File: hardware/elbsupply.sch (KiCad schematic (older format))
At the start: 69 parts

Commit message: changed pre-regulator to TPS54331DDA, need to calculate exact values
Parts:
- removed C?: 100uF, symbol CP1
- removed C?: CP1, symbol CP1
- removed D?: DIODESCH, symbol DIODESCH
- removed D?: 1N4148WS, symbol DIODE
- removed L?: INDUCTOR, symbol INDUCTOR
- removed Q?: KST2907A, symbol PNP
- removed R? (x3): 10k, symbol R
- removed U?: LM2576T-ADJ, TO220-5, symbol LM2576T-ADJ
- added C? (x6): C, symbol C
- added D?: DIODESCH, symbol DIODESCH
- added D?: 1N4148WS, symbol DIODE
- added L?: INDUCTOR, symbol INDUCTOR
- added Q?: KST2907A, symbol PNP
- added R?: 18k, symbol R
- added R? (x2): 10k, symbol R
- added R? (x3): R, symbol R
- added U?: TPS54331DDA, symbol TPS54331DDA
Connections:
- wire segments 263 -> 278
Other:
- note added: "Pre-regulator tracking control\nKeeps output voltage of TPS54331\nalways approx. 2V above LT3083\noutput voltage"
- note removed: "Pre-regulator tracking control\nKeeps output voltage of LM2576 \nalways approx. 1.9V above LT3083\noutput voltage"
- moved on the sheet: C?, CON?, D?, DS?, IC?, P?, R?, RP?, RV?, U?, U?A

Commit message: final Rev. A schematic
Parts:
- removed R? (x2): R, symbol R
- added C?: 4.7uF, symbol C
- added C? (x2): 22uF, symbol C
- C?: value C -> 0.1uF
- C?: value C -> 22uF
- C?: value C -> 390pF
- C?: value C -> 7pF
- C?: value C -> 8.2nF
- C?: value C -> 4.7uF
- D?: value DIODESCH -> SK54C
- D?: value TVS -> SM6T27A
- L?: value INDUCTOR -> 5.2uH
- R?: value R -> 73k2
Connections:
- net +24V: now also C?.2
- net GND: now also C?.1, C?.1, C?.1, C?.1; no longer C?.2
- net at C?.2, L?.2, R?.1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: now also C?.2, C?.2
- net at U?.4 (SS): now also C?.2; no longer C?.1
- no-connect marks 15 -> 16
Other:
- moved on the sheet: C?, D?, L?, P?, Q?, R?, RP?, U?, U?A

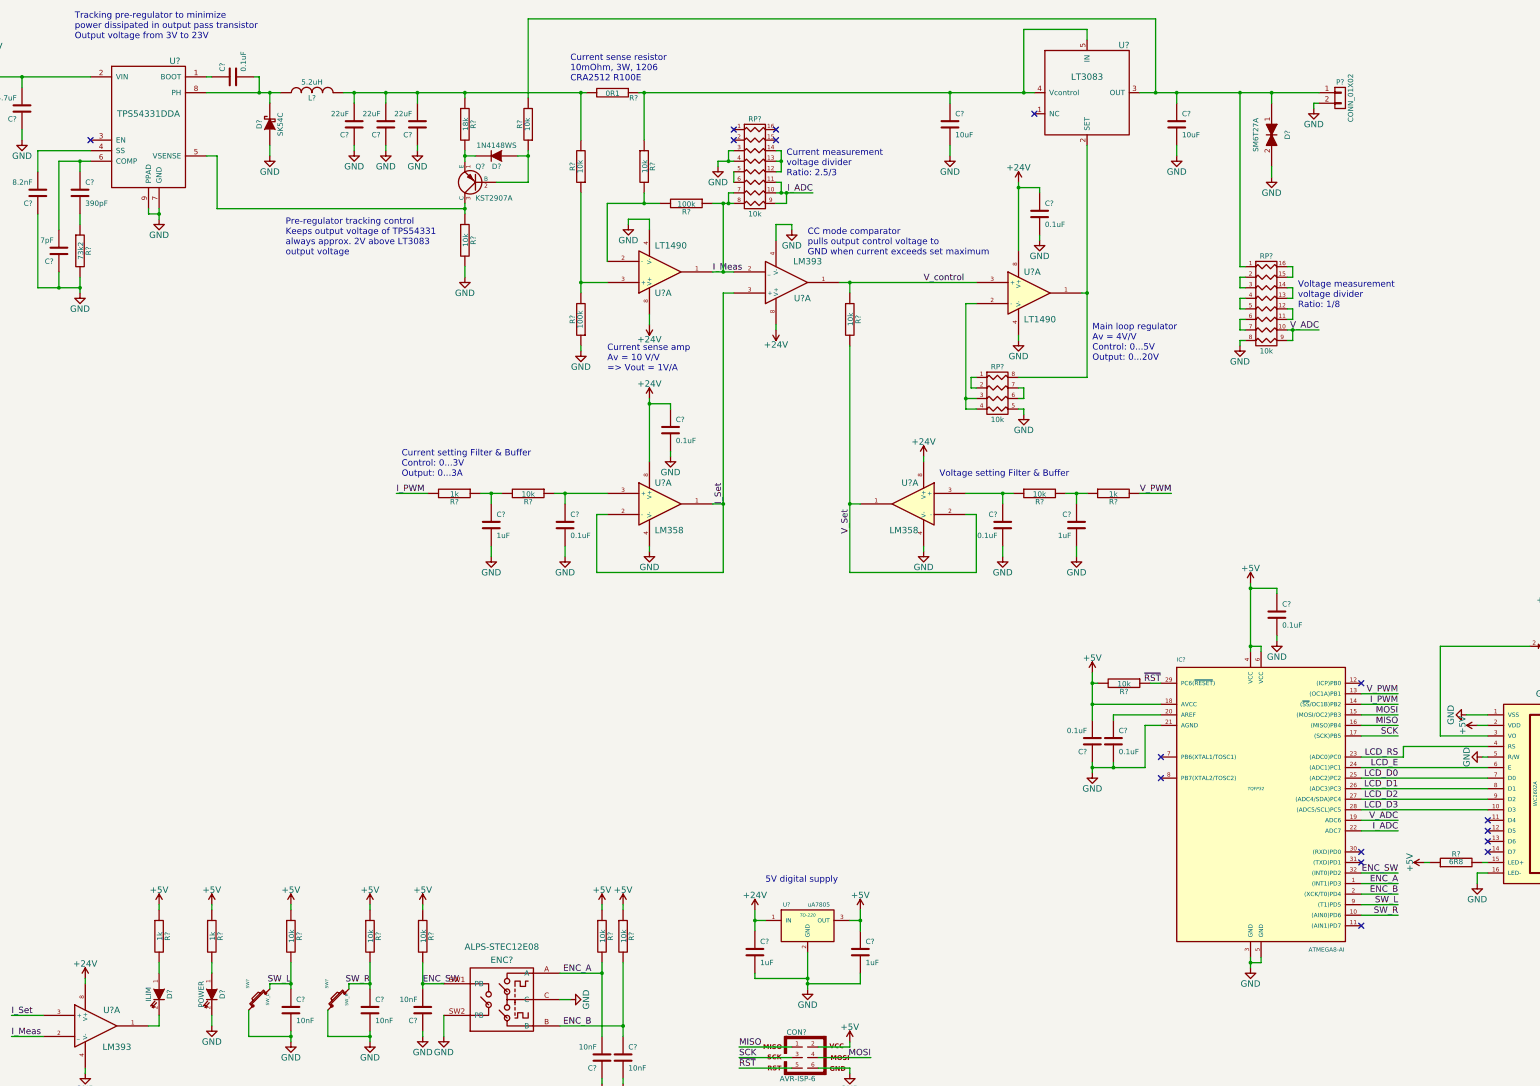
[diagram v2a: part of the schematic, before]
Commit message: changed 5V regulator for surface mount version
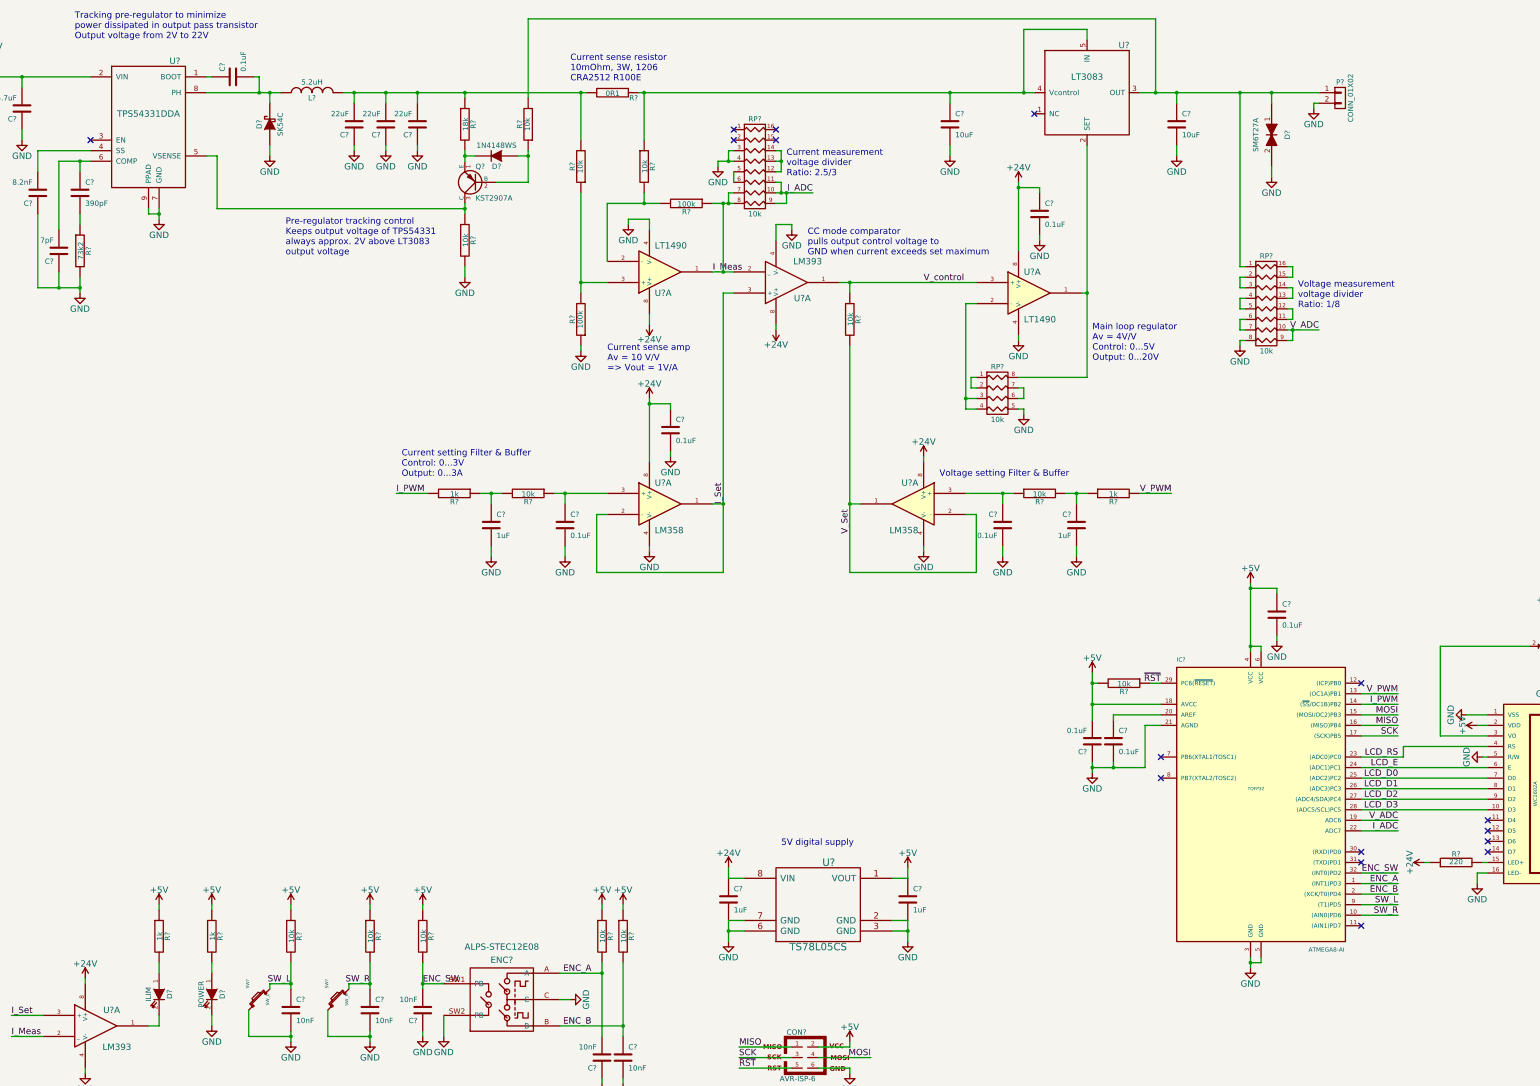
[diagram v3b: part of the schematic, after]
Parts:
- removed U?: uA7805, TO-220, symbol LM7805CT
- added U?: TS78L05CS, symbol 7805MS
- R?: value 6R8 -> 220
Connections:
- net +24V: now also R?.1, U?.8 (VIN)
- net +5V: now also U?.1 (VOUT); no longer R?.1
- net GND: now also U?.2 (GND), U?.3 (GND), U?.6 (GND), U?.7 (GND)
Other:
- note added: "Tracking pre-regulator to minimize\npower dissipated in output pass transistor\nOutput voltage from 2V to 22V"
- note removed: "Tracking pre-regulator to minimize\npower dissipated in output pass transistor\nOutput voltage from 3V to 23V"
- moved on the sheet: C?
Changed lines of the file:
@@
 P 14700 8700
 F 0 "R?" V 14780 8700 50  0000 C CNN
-F 1 "6R8" V 14707 8701 50  0000 C CNN
+F 1 "220" V 14707 8701 50  0000 C CNN
 F 2 "" V 14630 8700 30  0000 C CNN
 F 3 "" H 14700 8700 30  0000 C CNN
 	1    14700 8700
-	0    -1   -1   0
-$EndComp
-$Comp
-L +5V #PWR?
-U 1 1 54E37CA0
-P 14400 8700
-F 0 "#PWR?" H 14400 8550 60  0001 C CNN
-F 1 "+5V" H 14400 8840 60  0000 C CNN
-F 2 "" H 14400 8700 60  0000 C CNN
-F 3 "" H 14400 8700 60  0000 C CNN
-	1    14400 8700
 	0    -1   -1   0
 $EndComp
@@
 Pre-regulator tracking control\nKeeps output voltage of TPS54331\nalways approx. 2V above LT3083\noutput voltage
 Text Notes 1600 900  0    60   ~ 0
-Tracking pre-regulator to minimize\npower dissipated in output pass transistor\nOutput voltage from 3V to 23V
+Tracking pre-regulator to minimize\npower dissipated in output pass transistor\nOutput voltage from 2V to 22V
 $Comp
 L LM358 U?
@@
 CC mode comparator\npulls output control voltage to \nGND when current exceeds set maximum
 $Comp
-L LM7805CT U?
-U 1 1 54EA329A
-P 8550 9300
-F 0 "U?" H 8350 9500 40  0000 C CNN
-F 1 "uA7805" H 8550 9500 40  0000 L CNN
-F 2 "TO-220" H 8550 9400 30  0000 C CIN
-F 3 "" H 8550 9300 60  0000 C CNN
-	1    8550 9300
-	1    0    0    -1
-$EndComp
-$Comp
 L C C?
 U 1 1 54EA352A
-P 8050 9550
-F 0 "C?" H 8100 9650 50  0000 L CNN
-F 1 "1uF" H 8100 9450 50  0000 L CNN
-F 2 "" H 8088 9400 30  0000 C CNN
-F 3 "" H 8050 9550 60  0000 C CNN
-	1    8050 9550
+P 7800 9050
+F 0 "C?" H 7850 9150 50  0000 L CNN
+F 1 "1uF" H 7850 8950 50  0000 L CNN
+F 2 "" H 7838 8900 30  0000 C CNN
+F 3 "" H 7800 9050 60  0000 C CNN
+	1    7800 9050
 	1    0    0    -1
 $EndComp
@@
 L C C?
 U 1 1 54EA3597
-P 9050 9550
-F 0 "C?" H 9100 9650 50  0000 L CNN
-F 1 "1uF" H 9100 9450 50  0000 L CNN
-F 2 "" H 9088 9400 30  0000 C CNN
-F 3 "" H 9050 9550 60  0000 C CNN
-	1    9050 9550
+P 9500 9050
+F 0 "C?" H 9550 9150 50  0000 L CNN
+F 1 "1uF" H 9550 8950 50  0000 L CNN
+F 2 "" H 9538 8900 30  0000 C CNN
+F 3 "" H 9500 9050 60  0000 C CNN
+	1    9500 9050
 	1    0    0    -1
 $EndComp
@@
 L GND #PWR?
 U 1 1 54EA39E5
-P 8550 9900
-F 0 "#PWR?" H 8550 9650 60  0001 C CNN
-F 1 "GND" H 8550 9750 60  0000 C CNN
-F 2 "" H 8550 9900 60  0000 C CNN
-F 3 "" H 8550 9900 60  0000 C CNN
-	1    8550 9900
+P 7800 9450
+F 0 "#PWR?" H 7800 9200 60  0001 C CNN
+F 1 "GND" H 7800 9300 60  0000 C CNN
+F 2 "" H 7800 9450 60  0000 C CNN
+F 3 "" H 7800 9450 60  0000 C CNN
+	1    7800 9450
 	1    0    0    -1
 $EndComp
@@
 L +5V #PWR?
 U 1 1 54EA3FE5
-P 9050 9150
-F 0 "#PWR?" H 9050 9000 60  0001 C CNN
-F 1 "+5V" H 9050 9290 60  0000 C CNN
-F 2 "" H 9050 9150 60  0000 C CNN
-F 3 "" H 9050 9150 60  0000 C CNN
-	1    9050 9150
+P 9500 8750
+F 0 "#PWR?" H 9500 8600 60  0001 C CNN
+F 1 "+5V" H 9500 8890 60  0000 C CNN
+F 2 "" H 9500 8750 60  0000 C CNN
+F 3 "" H 9500 8750 60  0000 C CNN
+	1    9500 8750
 	1    0    0    -1
 $EndComp
@@
 L +24V #PWR?
 U 1 1 54EA4241
-P 8050 9150
-F 0 "#PWR?" H 8050 9000 60  0001 C CNN
-F 1 "+24V" H 8050 9290 60  0000 C CNN
-F 2 "" H 8050 9150 60  0000 C CNN
-F 3 "" H 8050 9150 60  0000 C CNN
-	1    8050 9150
+P 7800 8750
+F 0 "#PWR?" H 7800 8600 60  0001 C CNN
+F 1 "+24V" H 7800 8890 60  0000 C CNN
+F 2 "" H 7800 8750 60  0000 C CNN
+F 3 "" H 7800 8750 60  0000 C CNN
+	1    7800 8750
 	1    0    0    -1
 $EndComp
@@
 	1    0    0    -1
 $EndComp
-Text Notes 8150 8900 0    60   ~ 0
+Text Notes 8300 8550 0    60   ~ 0
 5V digital supply\n
 $Comp
@@
 	6650 2450 7150 2450
 Wire Wire Line
-	8550 9550 8550 9900
-Wire Wire Line
-	9050 9750 9050 9850
-Connection ~ 8550 9850
-Wire Wire Line
-	8550 9800 8050 9800
-Wire Wire Line
-	8050 9800 8050 9750
-Connection ~ 8550 9800
-Wire Wire Line
-	8050 9150 8050 9350
-Wire Wire Line
-	8050 9250 8150 9250
-Wire Wire Line
-	9050 9150 9050 9350
-Connection ~ 9050 9250
-Connection ~ 8050 9250
-Wire Wire Line
-	8950 9250 9050 9250
-Wire Wire Line
-	9050 9850 8550 9850
-Wire Wire Line
 	11250 7200 11900 7200
 Wire Wire Line
@@
 Connection ~ 1100 1250
 NoConn ~ 1750 1850
+$Comp
+L +24V #PWR?
+U 1 1 54F3C5A7
+P 14400 8700
+F 0 "#PWR?" H 14400 8550 60  0001 C CNN
+F 1 "+24V" H 14400 8840 60  0000 C CNN
+F 2 "" H 14400 8700 60  0000 C CNN
+F 3 "" H 14400 8700 60  0000 C CNN
+	1    14400 8700
+	0    -1   -1   0
+$EndComp
+$Comp
+L 7805MS U?
+U 1 1 54F3D9BD
+P 8650 9100
+F 0 "U?" H 8750 9500 70  0000 C CNN
+F 1 "TS78L05CS" H 8650 8700 70  0000 C CNN
+F 2 "" H 8650 9100 60  0000 C CNN
+F 3 "" H 8650 9100 60  0000 C CNN
+	1    8650 9100
+	1    0    0    -1
+$EndComp
+$Comp
+L GND #PWR?
+U 1 1 54F3EB33
+P 9500 9450
+F 0 "#PWR?" H 9500 9200 60  0001 C CNN
+F 1 "GND" H 9500 9300 60  0000 C CNN
+F 2 "" H 9500 9450 60  0000 C CNN
+F 3 "" H 9500 9450 60  0000 C CNN
+	1    9500 9450
+	1    0    0    -1
+$EndComp
+Wire Wire Line
+	7800 8750 7800 8850
+Wire Wire Line
+	7800 8850 7950 8850
+Wire Wire Line
+	7800 9250 7800 9450
+Wire Wire Line
+	7800 9250 7950 9250
+Wire Wire Line
+	7800 9350 7950 9350
+Connection ~ 7800 9350
+Wire Wire Line
+	9350 9250 9500 9250
+Wire Wire Line
+	9500 9250 9500 9450
+Wire Wire Line
+	9350 9350 9500 9350
+Connection ~ 9500 9350
+Wire Wire Line
+	9350 8850 9500 8850
+Wire Wire Line
+	9500 8850 9500 8750
 $EndSCHEMATC

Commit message: final Rev. A schematic annotated
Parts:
- gave numbers to parts that had none: 74
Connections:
- net I_Meas: now also U1.6 (_); no longer U1.2 (_)
- net I_Set: now also U1.5 (+); no longer U1.3 (+)
- net V_Set: now also U4.6 (-), U4.7; no longer U4.1, U4.2 (-)
- net V_control: now also U1.7, U3.5 (+); no longer U1.1, U3.3 (+)
- net at C21.1, R20.1: now also U4.5 (+); no longer U4.3 (+)
- net at RP2.8 (R1), U6.2 (SET): now also U3.7; no longer U3.1
- net at RP2.3 (P3), RP2.4 (P4): now also U3.6 (-); no longer U3.2 (-)

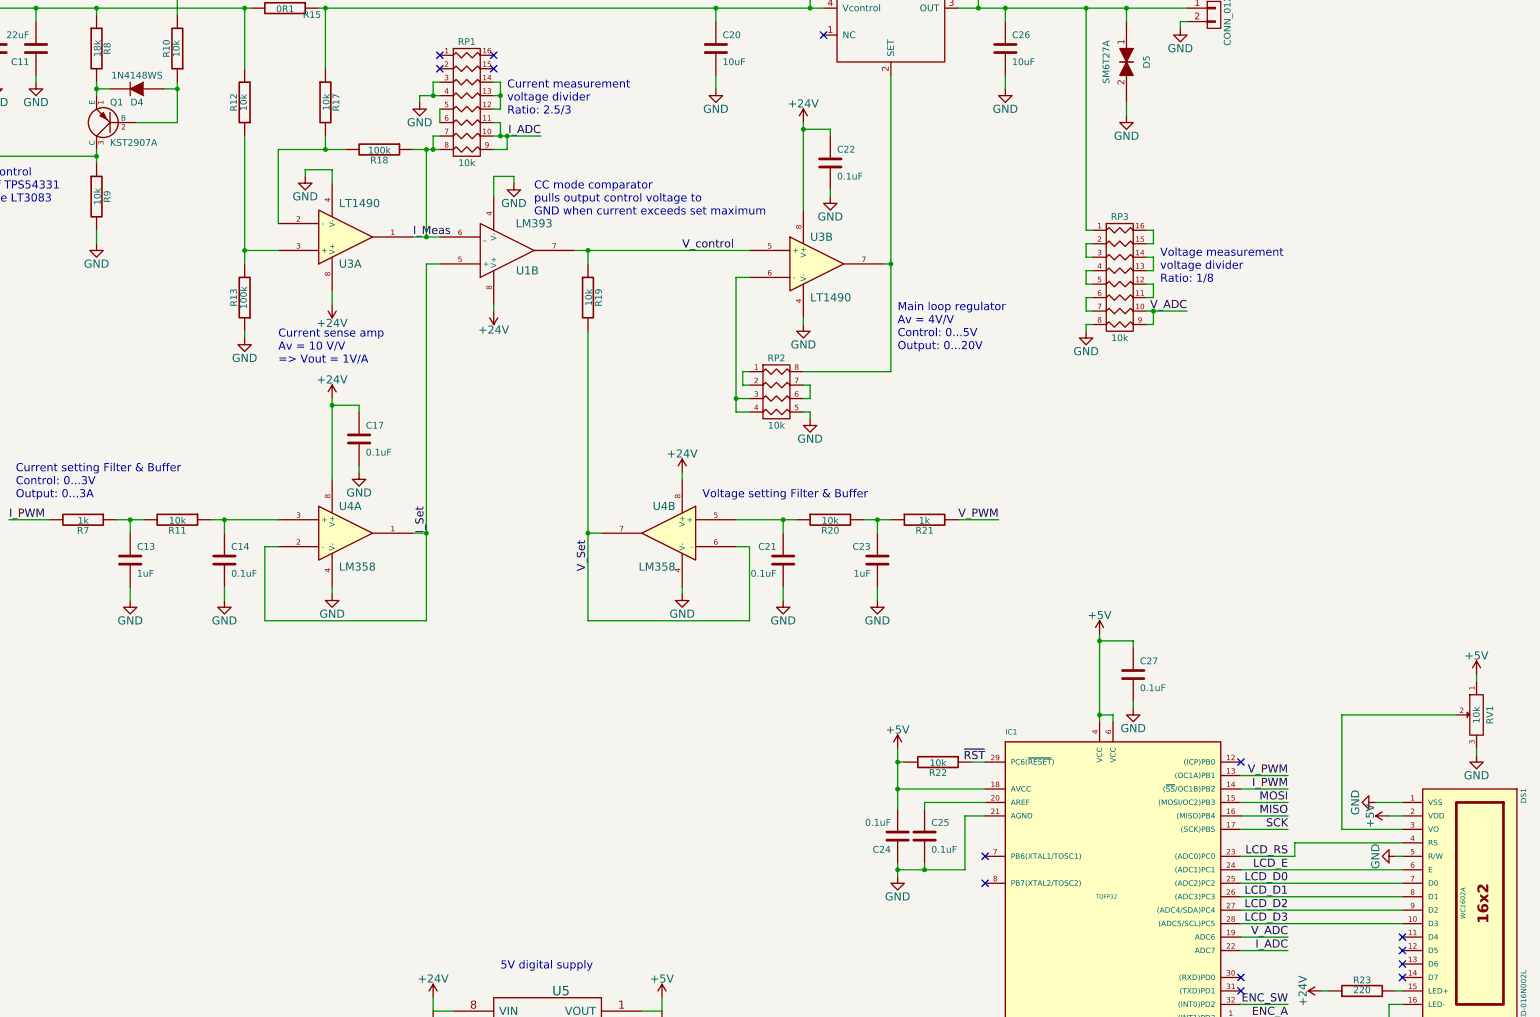
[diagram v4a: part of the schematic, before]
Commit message: partially done with footprint association
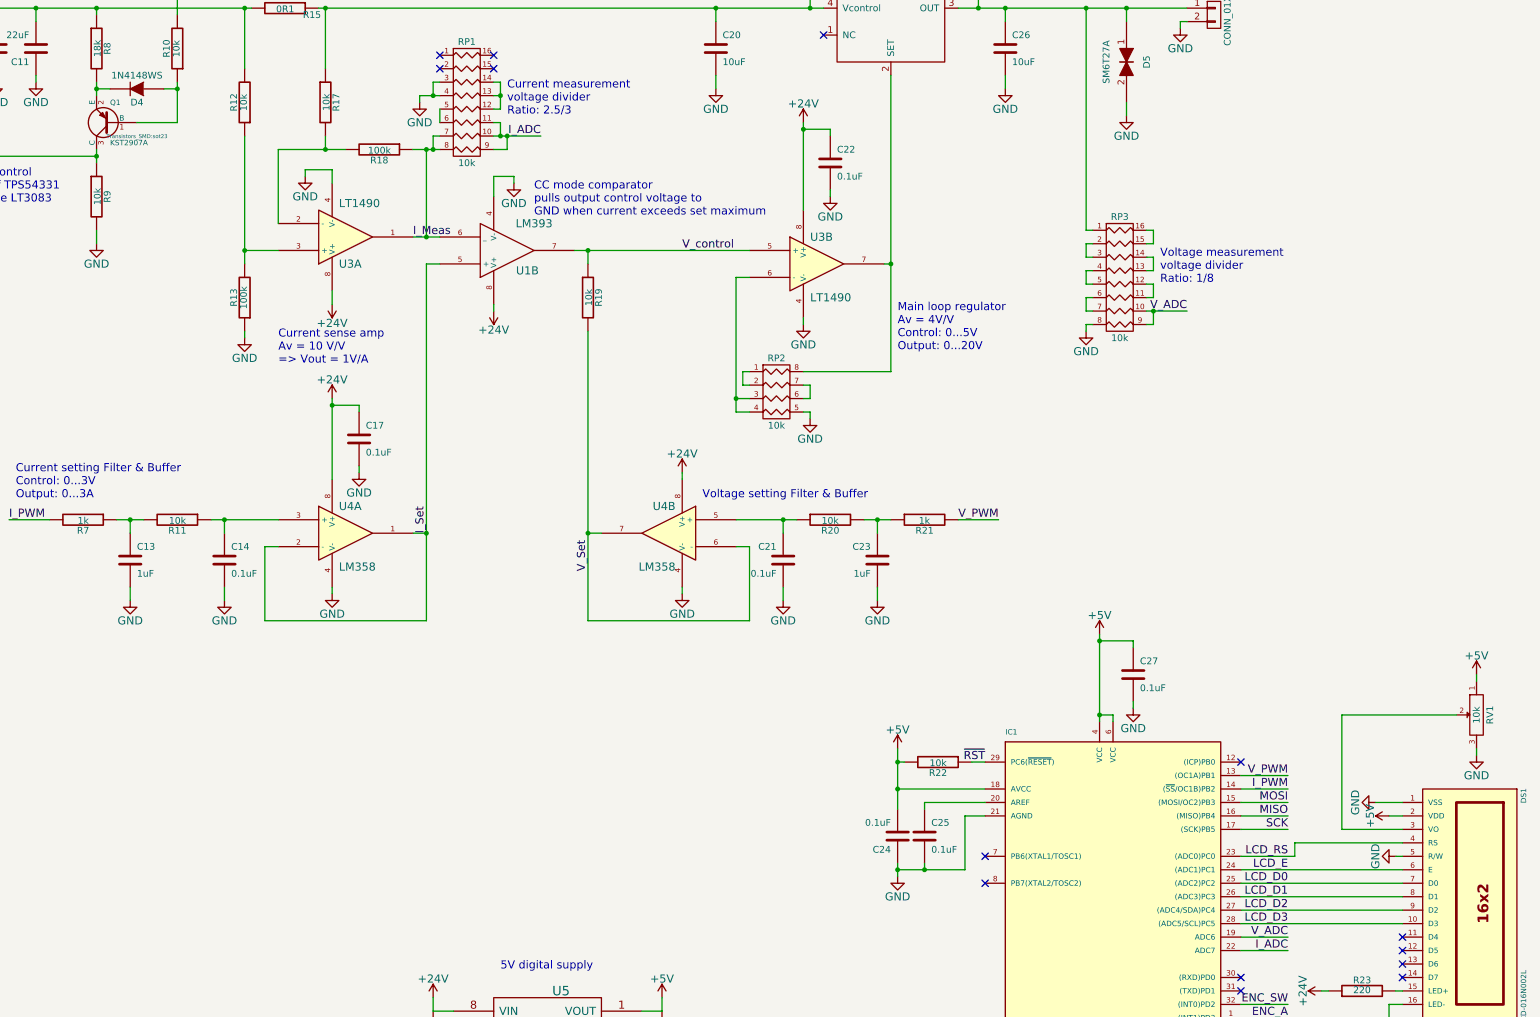
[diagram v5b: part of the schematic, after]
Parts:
- removed Q1: KST2907A, symbol PNP
- added Q1: KST2907A, Transistors_SMD:sot23, symbol BC808-40
- C1, C10, C11, C12, C13, C14, C15, C16, C17, C18, C19, C2, C20, C21, C22, C23, C24, C25, C26, C27, C3, C4, C5, C6, C7, C8, C9: footprint (none) -> Capacitors_SMD:C_0805_HandSoldering
- CON1: footprint AVR-ISP-6 -> Pin_Headers:Pin_Header_Straight_2x03
- D1, D2: footprint (none) -> LEDs:LED-0805
- D3: footprint (none) -> Diodes_SMD:Diode-SMC_Handsoldering
- D4: footprint (none) -> Diodes_SMD:SOD-323
- D5: footprint (none) -> Diodes_SMD:Diode-SMB_Handsoldering
- DS1: footprint WC1602A -> (none)
- IC1: footprint TQFP32 -> Housings_QFP:TQFP-32_7x7mm_Pitch0.8mm
- R1, R10, R11, R12, R13, R14, R15, R16, R17, R18, R19, R2, R20, R21, R22, R23, R3, R4, R5, R6, R7, R8, R9: footprint (none) -> Resistors_SMD:R_0805_HandSoldering
- U1, U3, U4, U5: footprint (none) -> Housings_SOIC:SOIC-8_3.9x4.9mm_Pitch1.27mm
- U2: footprint (none) -> Housings_SOIC:SOIC-8-1EP_3.9x4.9mm_Pitch1.27mm
- U6: footprint (none) -> Pentawatts:Pentawatt_Neutral_Staggered_Verical_TO220-5-T05D
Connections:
- net at R9.1, U2.5 (VSENSE): now also Q1.3 (C)
- net at D4.2 (K), R8.2: now also Q1.2 (E)
- net at D4.1 (A), R10.1: now also Q1.1 (B)
